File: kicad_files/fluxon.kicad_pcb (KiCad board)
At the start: 2 copper layers, 241.6 x 71.7 mm, 157 parts, among them J1 ARM SWD, J2 U-F-M5DD-W-2, J3 Conn_02x10, Q1 BSS138, Q2 MUN5335DW1T1G, SW1 ESC, SW10 O, SW11 P, SW12 DEL, SW13 TAB_125, SW14 A, SW15 S, SW16 D, SW17 F, SW18 G, SW19 H, SW2 Q, SW20 J, SW21 K, SW22 L, SW23 QUOTE, SW24 ENTER_175, SW25 LSHIFT_175, SW26 Z, SW27 X, SW28 C, SW29 V, SW3 W, SW30 B, SW31 N, SW32 M, SW33 COMMA, SW34 DOT, SW35 (D) RSHIFT_125, SW36 (D) FN_100, SW37 (F) RSHIFT_225, SW38 (I) RSHIFT_125, SW39 (I) SLASH_100, SW4 E, SW40 LCTRL_125, SW41 SUPER_100, SW42 LALT_100, SW43 SPC_625, SW44 RALT_125, SW45 RGUI_100, SW46 RCTRL_125, SW47 BKSP, SW48 BKSP_2U, SW49 PN_100, SW5 R, SW50 SPC_175, SW51 SPC_275, SW52 FN_100, SW53 RALT_100, SW54 LCTRL_150, SW55 LALT_150, SW56 SPC_700, SW57 RCTRL_150, SW58 RALT_150, SW6 T, SW7 Y, SW8 U, SW9 I, U1 USBLC6-2SC6, U2 MCP1700-3302E/TT, U3 STM32L072CBT6

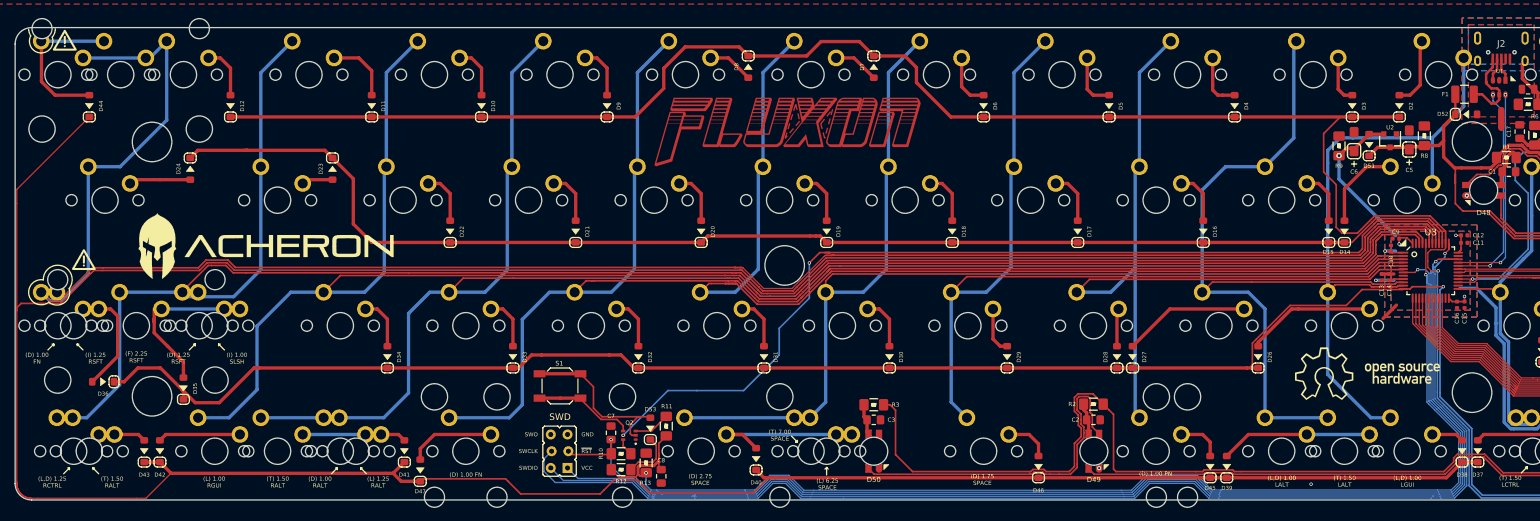
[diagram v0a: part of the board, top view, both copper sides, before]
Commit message: Silkscreen and tracing improvements
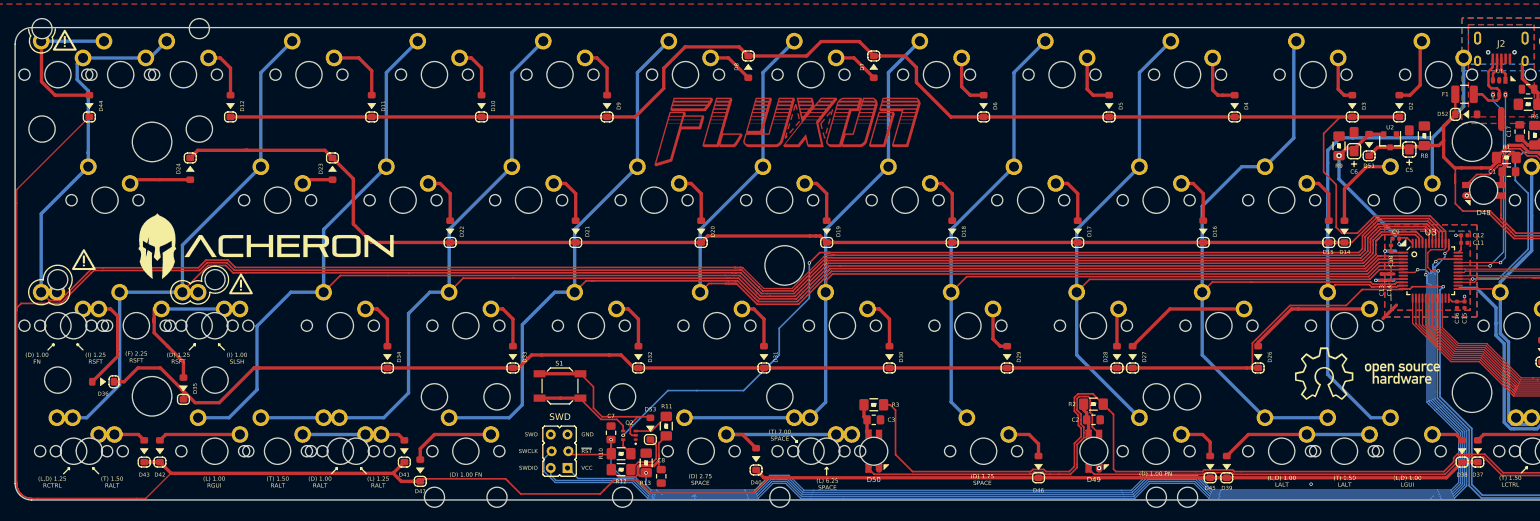
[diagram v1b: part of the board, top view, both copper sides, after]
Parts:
- added GR7: Warning Sign, acheron_Graphics:warning_sign_3.6x3.2mm, F.Cu at (63.2, 96.9)
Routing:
- net Col12: track 292.5 -> 280.0 mm
- net Col3: track 115.6 -> 110.0 mm
- net Col11: track 285.1 -> 279.9 mm
- net Col8: track 213.0 -> 209.4 mm
- net Col10: track 255.7 -> 252.2 mm
- net Col6: track 179.2 -> 176.0 mm
- net Col5: track 137.3 -> 134.3 mm
- net Col9: track 246.1 -> 243.2 mm
- net Col7: track 160.0 -> 157.1 mm
- net Col4: track 121.4 -> 119.2 mm
- net VBUS: track 12.9 -> 11.8 mm
- net SWDIO: track 189.2 -> 189.8 mm
